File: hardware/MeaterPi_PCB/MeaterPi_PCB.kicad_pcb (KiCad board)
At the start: 2 copper layers, 60 x 40 mm, 18 parts, among them J1 12V_BARREL_JACK, J2 RASPBERRY_PI_GPIO, J3 ENV_III, J4 4PIN_PWM_FAN, Q1 2N7002, Q2 PMOS_REV_PROTECT, U1 5V_BUCK_MODULE

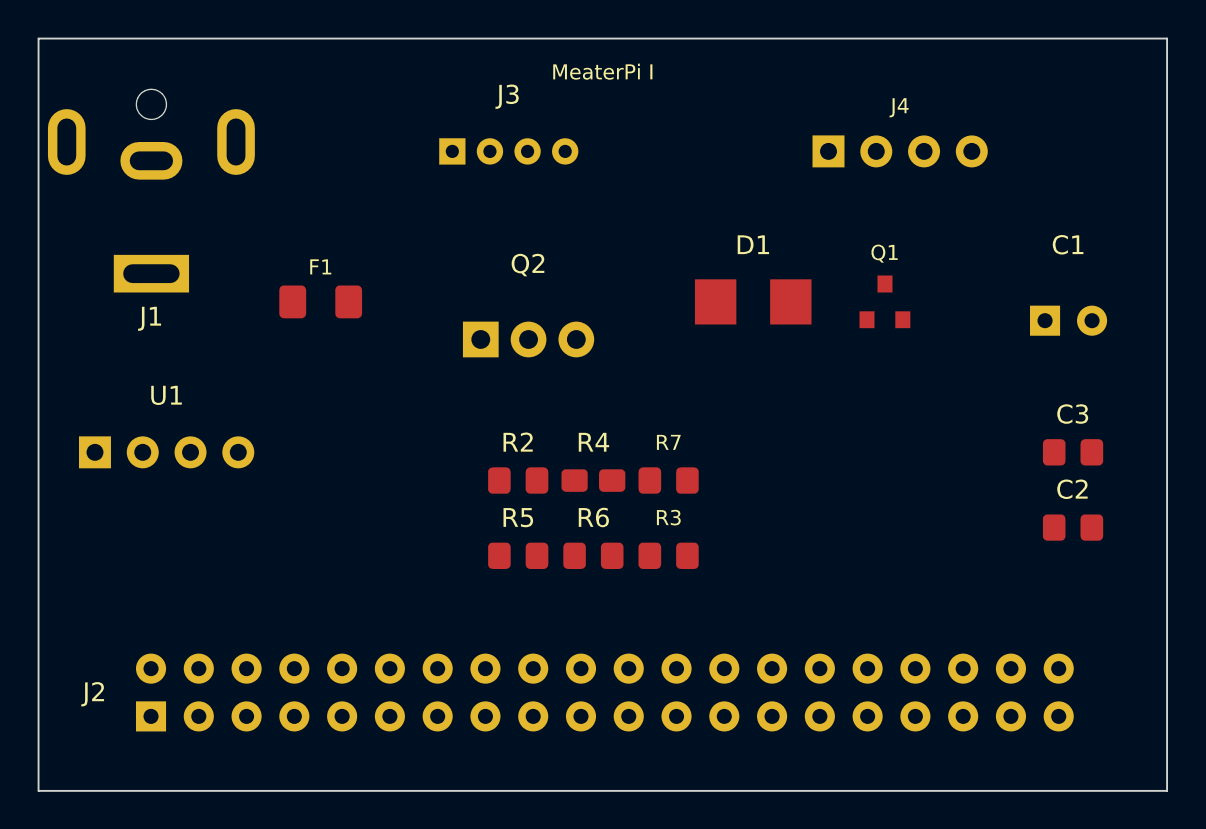
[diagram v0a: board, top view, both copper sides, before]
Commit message: smaller version wirh power extrnal
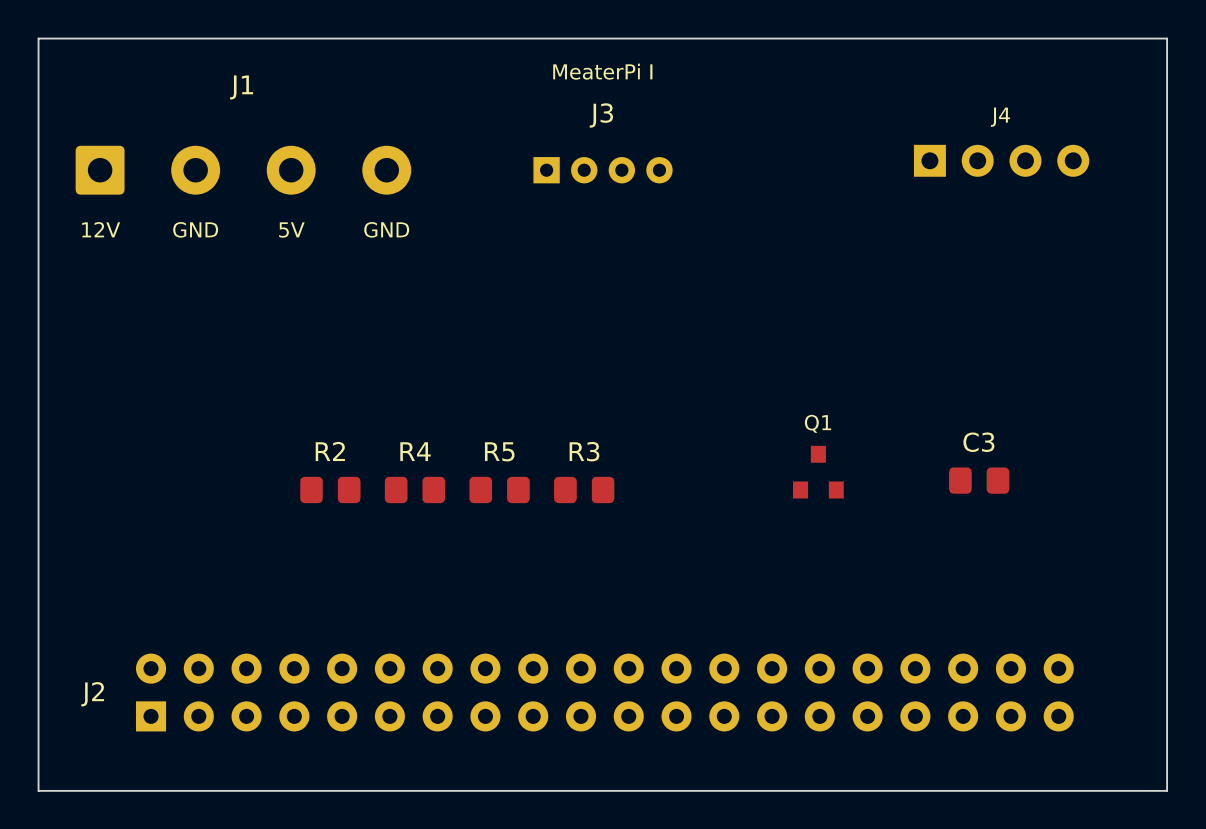
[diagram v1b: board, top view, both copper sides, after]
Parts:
- removed C1: 220uF/25V, Capacitor_THT:CP_Radial_D6.3mm_P2.50mm
- removed C2: 100nF, Capacitor_SMD:C_0805_2012Metric
- removed D1: SMBJ15A, Diode_SMD:D_SMB
- removed F1: SMD Polyfuse, Fuse:Fuse_1206_3216Metric_Pad1.42x1.75mm_HandSolder
- removed Q2: PMOS_REV_PROTECT, Package_TO_SOT_THT:TO-220-3_Vertical
- removed R6: 2k, Resistor_SMD:R_0805_2012Metric
- removed R7: 100k, Resistor_SMD:R_0805_2012Metric
- removed U1: 5V_BUCK_MODULE, Module:Buck_Converter_1x04_P2.54mm_Placeholder
- J1: value 12V_BARREL_JACK -> POWER_FROM_XY3606; footprint Connector_BarrelJack:BarrelJack_CUI_PJ-063AH_Horizontal -> TerminalBlock_Phoenix:TerminalBlock_Phoenix_MKDS-1,5-4-5.08_1x04_P5.08mm_Horizontal
- R4: value 10k DNP -> 10k
- moved R2 10.0 mm to (35.0, 42.5)
- moved Q1 9.72 mm to (61.0, 41.5)
- moved R4 9.50 mm to (39.5, 42.5)
- moved J1 6.14 mm to (22.8, 25.5), turned to 0 degrees
- moved R3 5.69 mm to (48.5, 42.5)
- moved J4 5.42 mm to (66.9, 25.0)
- moved C3 5.21 mm to (69.5, 42.0)
- moved J3 5.11 mm to (46.5, 25.5)
- moved R5 3.64 mm to (44.0, 42.5)
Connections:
- net FAN_PWM_GPIO17 renamed GPIO17
- net FAN_TACH_GPIO27 renamed GPIO27
- net SCL renamed ENV3_SCL
- net SDA renamed ENV3_SDA
- J1 pad 1: +12V_IN -> +12V_EXT
- J4 pad 2: +12V_PROT -> +12V_EXT

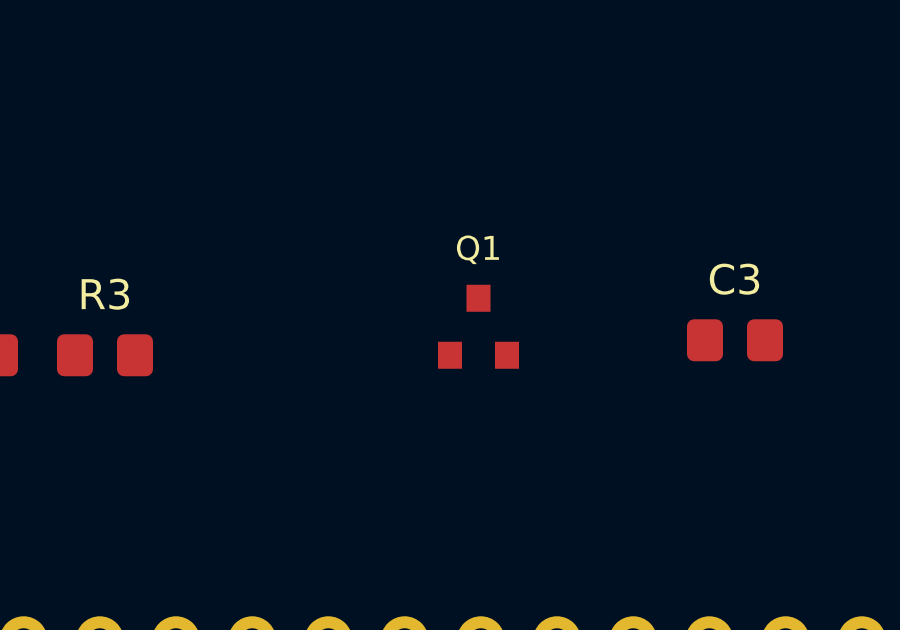
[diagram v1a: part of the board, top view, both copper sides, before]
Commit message: added schema for fan
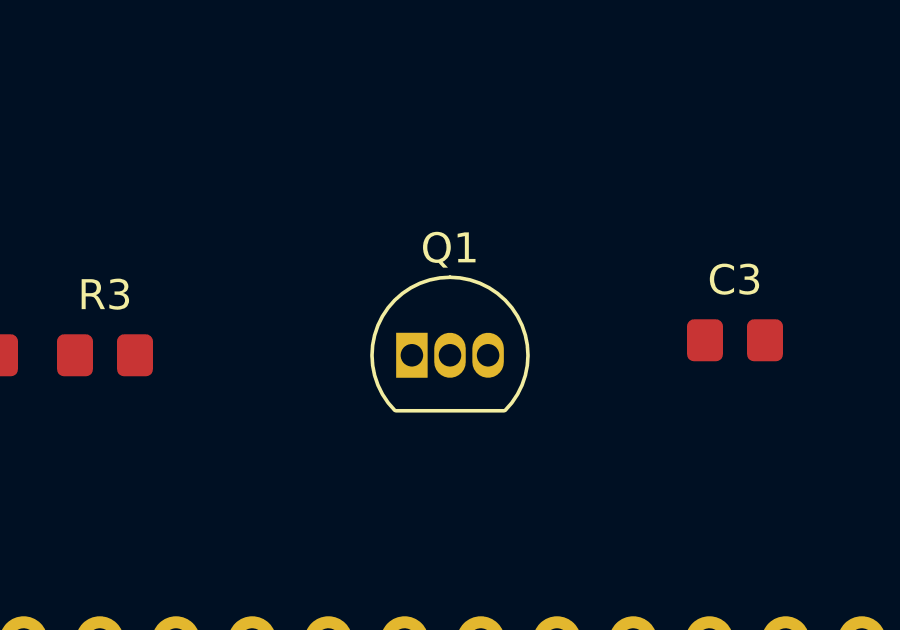
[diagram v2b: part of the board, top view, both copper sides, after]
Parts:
- Q1: value 2N7002 -> 2N3904; footprint Package_TO_SOT_SMD:SOT-23 -> Package_TO_SOT_THT:TO-92_Inline
- R2: value 220R -> 4.7k
- moved Q1 2.41 mm to (58.7, 42.5)
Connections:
- Q1 pad 1: FAN_PWM_GATE -> GND
- Q1 pad 2: GND -> Q1_BASE
- R2 pad 2: FAN_PWM_GATE -> Q1_BASE
- R3 pad 1: FAN_PWM_GATE -> Q1_BASE
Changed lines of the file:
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@@
 			)
 		)
-		(property "Value" "220R"
+		(property "Value" "4.7k"
 			(at 0 2.5 0)
 			(layer "F.Fab")
@@
 			(layers "F.Cu" "F.Mask" "F.Paste")
 			(roundrect_rratio 0.2)
-			(net "FAN_PWM_GATE")
+			(net "Q1_BASE")
 			(pinfunction "2")
 			(pintype "passive")
@@
 		)
 	)
-	(footprint "Package_TO_SOT_SMD:SOT-23"
+	(footprint "Package_TO_SOT_THT:TO-92_Inline"
 		(layer "F.Cu")
-		(at 60.95 41.55)
+		(at 58.73 42.5)
 		(property "Reference" "Q1"
-			(at 0 -2.6 0)
+			(at 1.27 -3.56 0)
 			(layer "F.SilkS")
 			(effects
 				(font
-					(size 0.8 0.8)
-					(thickness 0.12)
-				)
-			)
-		)
-		(property "Value" "2N7002"
-			(at 0 2.6 0)
+					(size 1 1)
+					(thickness 0.15)
+				)
+			)
+		)
+		(property "Value" "2N3904"
+			(at 1.27 2.79 0)
 			(layer "F.Fab")
 			(effects
@@
 		)
 		(duplicate_pad_numbers_are_jumpers no)
-		(pad "1" smd rect
-			(at -0.95 0.95)
-			(size 0.8 0.9)
-			(layers "F.Cu" "F.Mask" "F.Paste")
-			(net "FAN_PWM_GATE")
-			(pinfunction "G")
+		(fp_line
+			(start -0.53 1.85)
+			(end 3.07 1.85)
+			(stroke
+				(width 0.12)
+				(type solid)
+			)
+			(layer "F.SilkS")
+		)
+		(fp_arc
+			(start -0.568478 1.838478)
+			(mid -1.132087 -0.994977)
+			(end 1.27 -2.6)
+			(stroke
+				(width 0.12)
+				(type solid)
+			)
+			(layer "F.SilkS")
+		)
+		(fp_arc
+			(start 1.27 -2.6)
+			(mid 3.672087 -0.994977)
+			(end 3.108478 1.838478)
+			(stroke
+				(width 0.12)
+				(type solid)
+			)
+			(layer "F.SilkS")
+		)
+		(fp_text user "${REFERENCE}"
+			(at 1.27 0 0)
+			(layer "F.Fab")
+			(effects
+				(font
+					(size 1 1)
+					(thickness 0.15)
+				)
+			)
+		)
+		(pad "1" thru_hole rect
+			(at 0 0)
+			(size 1.05 1.5)
+			(drill 0.75)
+			(layers "*.Cu" "*.Mask")
+			(remove_unused_layers no)
+			(net "GND")
+			(pinfunction "E")
+			(pintype "passive")
+		)
+		(pad "2" thru_hole oval
+			(at 1.27 0)
+			(size 1.05 1.5)
+			(drill 0.75)
+			(layers "*.Cu" "*.Mask")
+			(remove_unused_layers no)
+			(net "Q1_BASE")
+			(pinfunction "B")
 			(pintype "input")
 		)
-		(pad "2" smd rect
-			(at 0.95 0.95)
-			(size 0.8 0.9)
-			(layers "F.Cu" "F.Mask" "F.Paste")
-			(net "GND")
-			(pinfunction "S")
+		(pad "3" thru_hole oval
+			(at 2.54 0)
+			(size 1.05 1.5)
+			(drill 0.75)
+			(layers "*.Cu" "*.Mask")
+			(remove_unused_layers no)
+			(net "FAN_PWM_OD")
+			(pinfunction "C")
 			(pintype "passive")
 		)
-		(pad "3" smd rect
-			(at 0 -0.95)
-			(size 0.8 0.9)
-			(layers "F.Cu" "F.Mask" "F.Paste")
-			(net "FAN_PWM_OD")
-			(pinfunction "D")
-			(pintype "passive")
-		)
 		(embedded_fonts no)
-		(model "${KICAD10_3DMODEL_DIR}/Package_TO_SOT_SMD.3dshapes/SOT-23.step"
+		(model "${KICAD10_3DMODEL_DIR}/Package_TO_SOT_THT.3dshapes/TO-92_Inline.step"
 			(offset
 				(xyz 0 0 0)
@@
 			(layers "F.Cu" "F.Mask" "F.Paste")
 			(roundrect_rratio 0.2)
-			(net "FAN_PWM_GATE")
+			(net "Q1_BASE")
 			(pinfunction "1")
 			(pintype "passive")
